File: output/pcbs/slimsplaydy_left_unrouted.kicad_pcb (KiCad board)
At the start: 2 copper layers, 117.1 x 87.4 mm, 24 parts

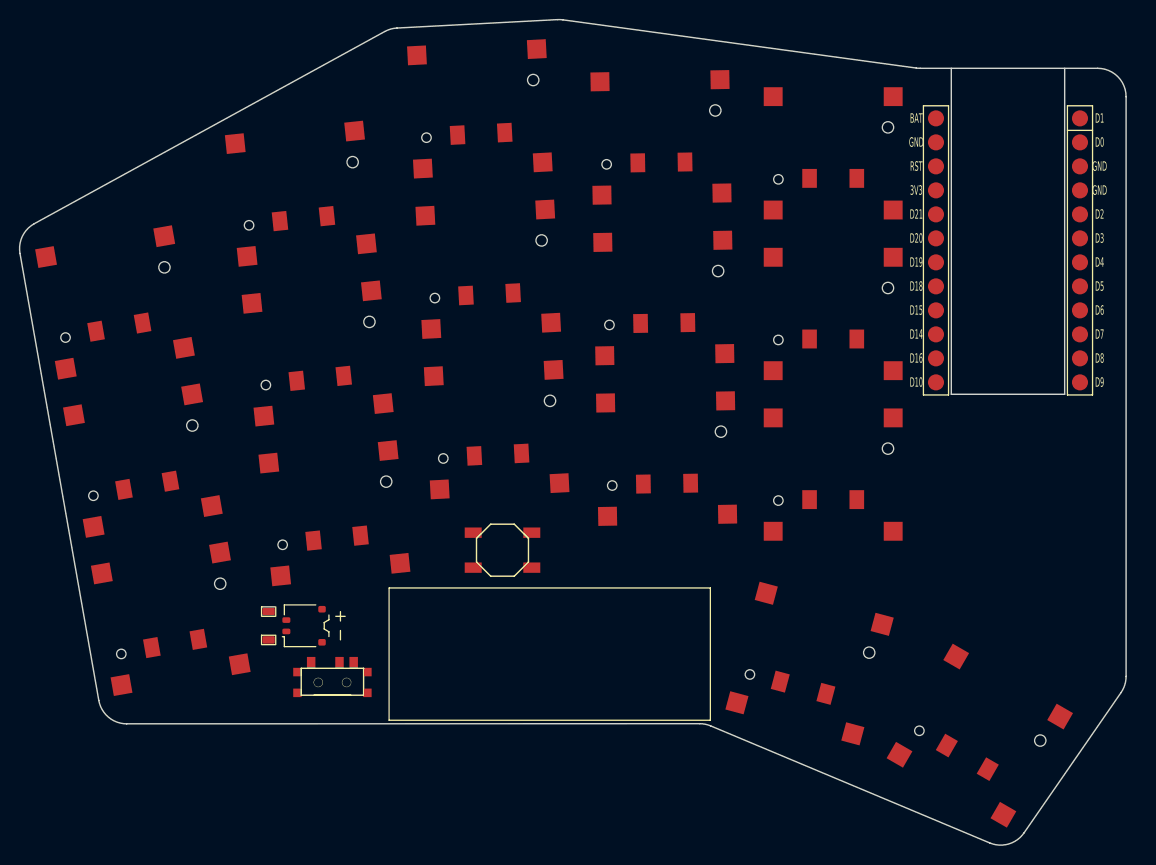
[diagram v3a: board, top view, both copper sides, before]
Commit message: Add new reversable PG1316S footprint.
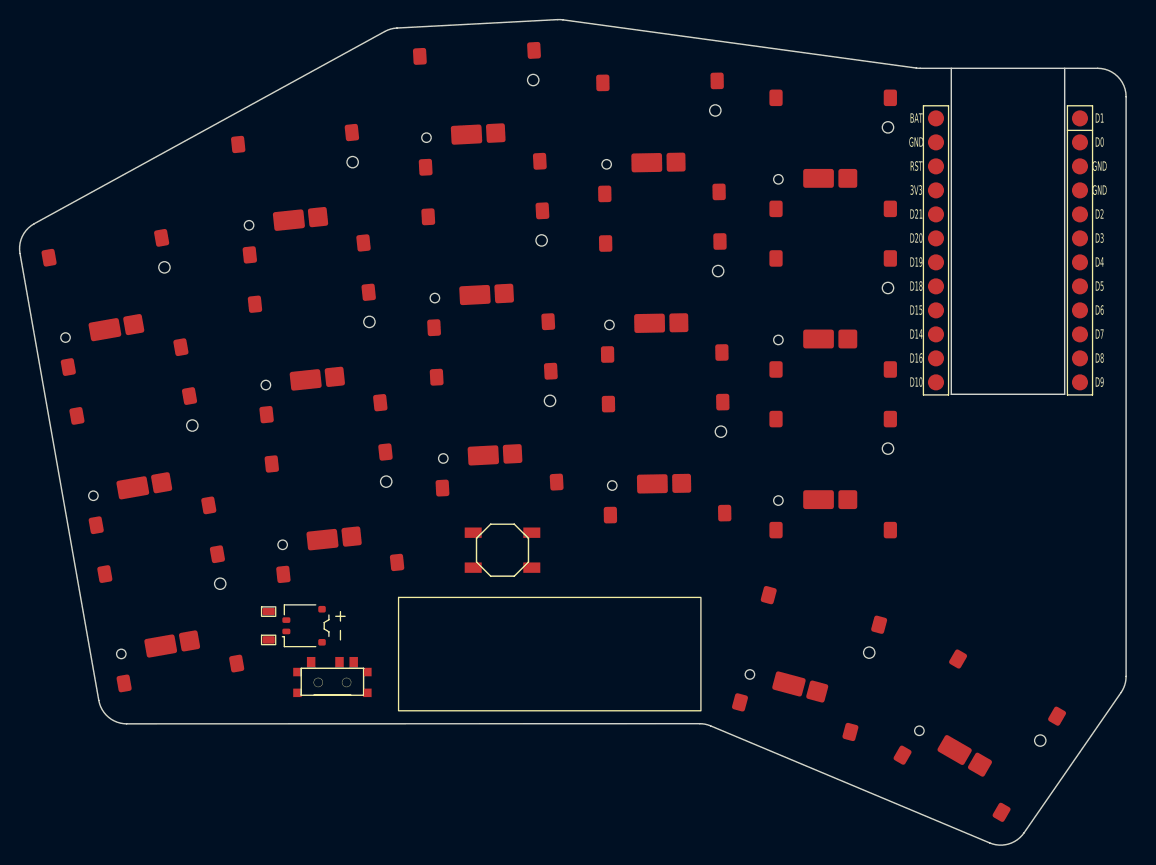
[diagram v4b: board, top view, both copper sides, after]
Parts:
- S1, S10, S11, S12, S13, S14, S15, S16, S17, S2, S3, S4, S5, S6, S7, S8, S9: footprint CPG1316S01D02_mikeholscher -> PG1316S
